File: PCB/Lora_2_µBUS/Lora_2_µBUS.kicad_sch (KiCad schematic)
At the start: 2 parts

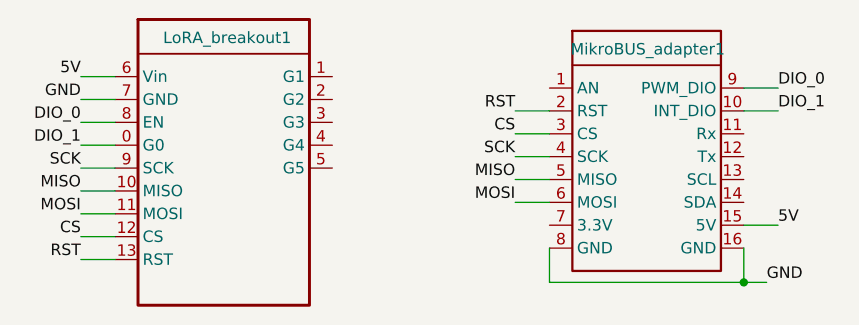
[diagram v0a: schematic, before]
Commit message: Updated µBus adapter
power redirected to 3.3V
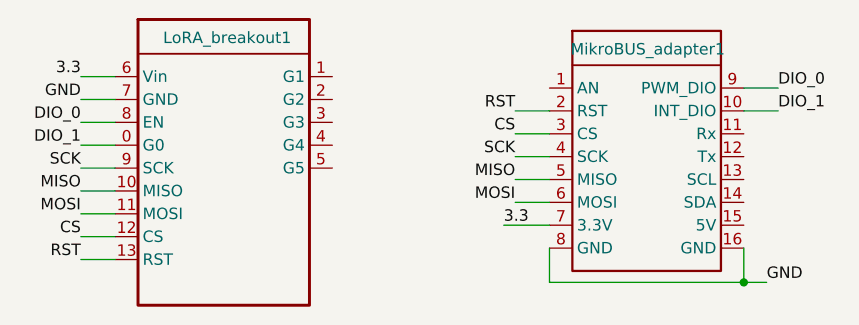
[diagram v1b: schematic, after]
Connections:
- net 3.3: now reaches MikroBUS_adapter1.7 (3.3V)
- net 3.3: now also LoRA_breakout1.6 (Vin)
- net 5V: no longer names the net of MikroBUS_adapter1.15 (5V)
- net 5V: no longer LoRA_breakout1.6 (Vin)
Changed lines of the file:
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@@
-	(wire
-		(pts
-			(xy 179.07 104.14) (xy 182.88 104.14)
-		)
-		(stroke
-			(width 0)
-			(type default)
-		)
-	)
 	(wire
 		(pts
@@
 	(wire
 		(pts
+			(xy 157.48 104.14) (xy 152.4 104.14)
+		)
+		(stroke
+			(width 0)
+			(type default)
+		)
+	)
+	(wire
+		(pts
 			(xy 153.67 91.44) (xy 157.48 91.44)
 		)
@@
 		)
 	)
-	(label "5V"
+	(label "3.3"
 		(at 105.41 87.63 180)
 		(fields_autoplaced yes)
@@
 		)
 	)
-	(label "5V"
-		(at 182.88 104.14 0)
-		(fields_autoplaced yes)
-		(effects
-			(font
-				(size 1.27 1.27)
-			)
-			(justify left bottom)
-		)
-	)
 	(label "SCK"
 		(at 153.67 96.52 180)
@@
 		)
 	)
+	(label "3.3"
+		(at 152.4 104.14 0)
+		(fields_autoplaced yes)
+		(effects
+			(font
+				(size 1.27 1.27)
+			)
+			(justify left bottom)
+		)
+	)
